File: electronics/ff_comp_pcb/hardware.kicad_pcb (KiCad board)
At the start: 4 copper layers, 60 x 37 mm, 92 parts, among them J1 Micro_SD_Card_Det_Hirose_DM3AT, J2 USB_A, J3 Conn_01x08_Female, U1 AS4C512M16D3L-12BIN, U2 A33, U3 FSUSB42MUX, U4 RTL8188CUS, U5 RTL8188CUS, Y1 24Mhz, Y2 32.768khz

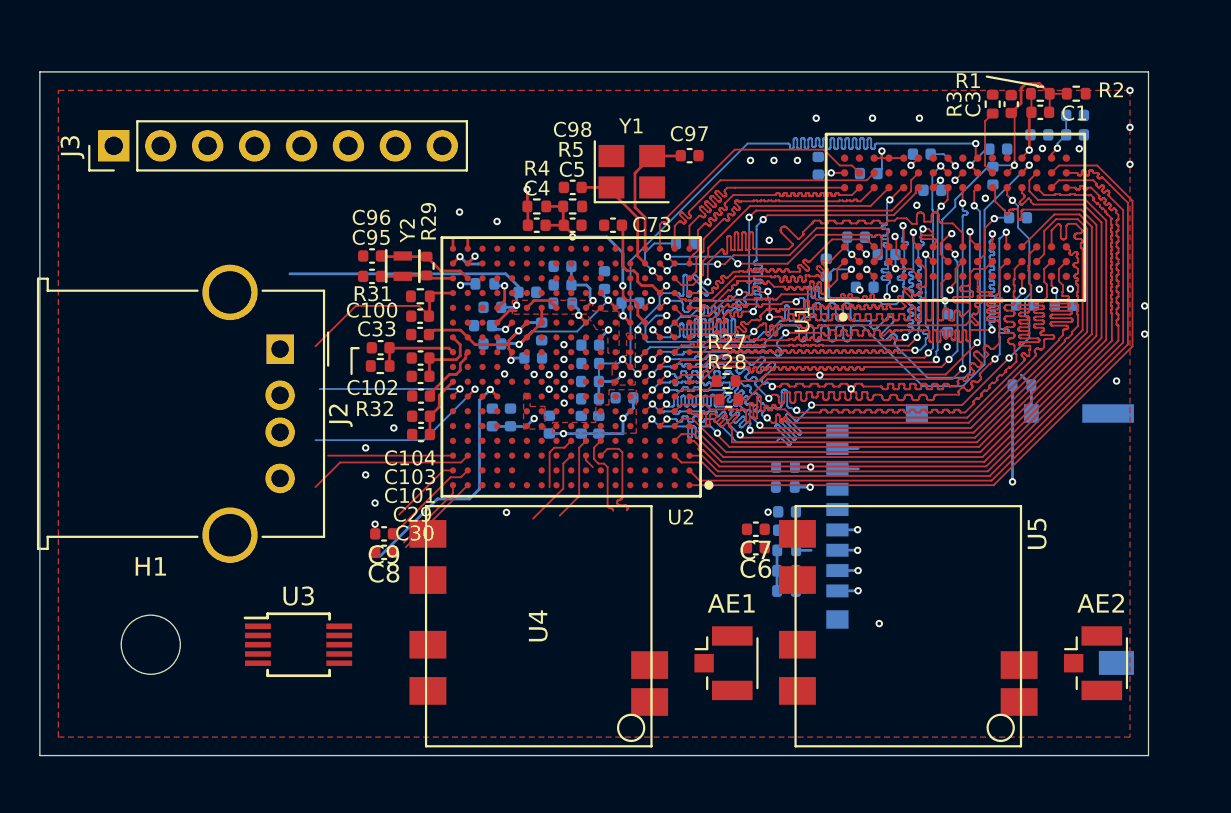
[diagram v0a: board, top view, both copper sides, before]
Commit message: Fit the board into the volume
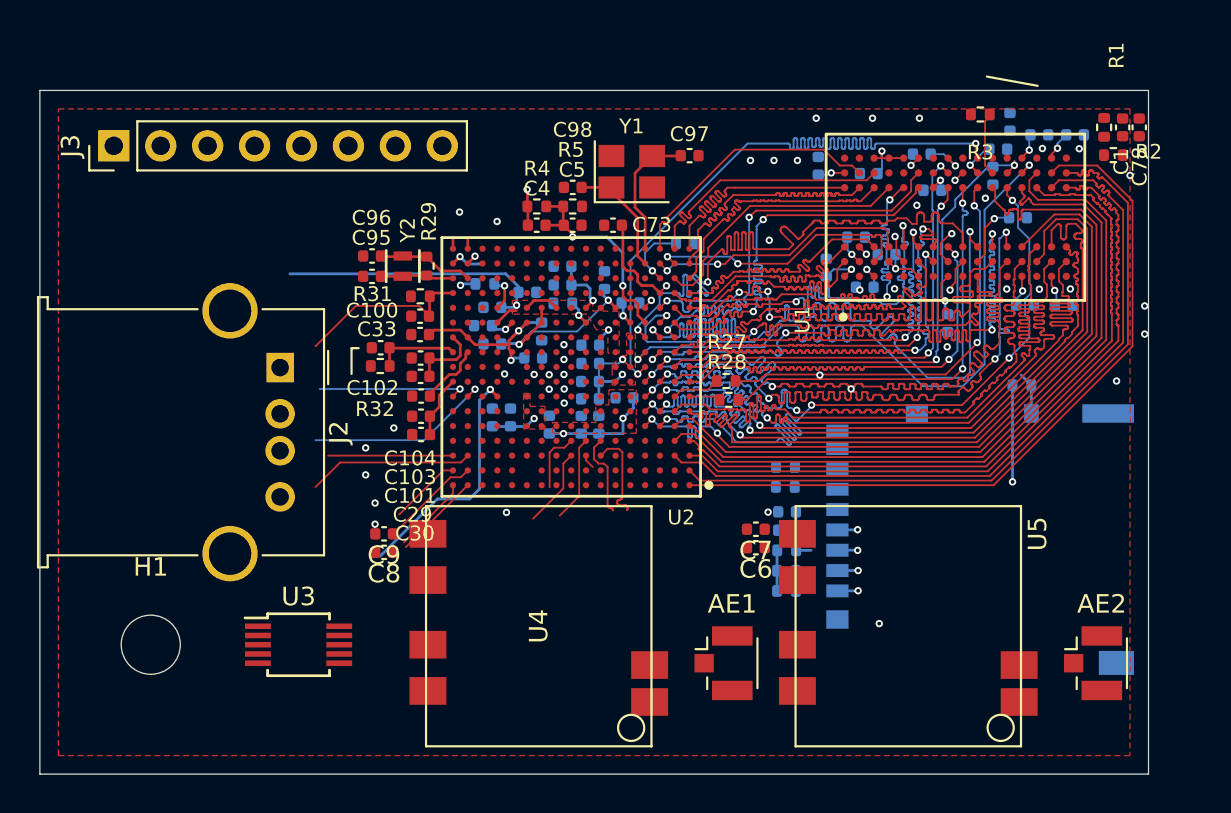
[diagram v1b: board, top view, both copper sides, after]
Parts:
- C3: moved to B.Cu
- C78: moved to F.Cu
- moved C1 4.53 mm to (144.6, 96.0), turned to 270 degrees
- moved R1 3.91 mm to (143.6, 96.0), turned to 270 degrees
- moved R2 3.88 mm to (144.1, 97.5)
- moved C78 3.54 mm to (145.5, 96.0), turned to 270 degrees
- moved J2 1.00 mm to (99.0, 109.0)
- moved C3 0.96 mm to (138.5, 95.7)
- moved R3 0.87 mm to (136.9, 95.3), turned to 0 degrees
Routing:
- net Net-(C1-Pad2): track 21.0 -> 13.0 mm
- net +1V35: track 43.1 -> 38.9 mm
- net /gpio/SD_DAT0: track 6.26 -> 4.29 mm, vias 1 -> 0
- net /gpio/SD_DAT1: track 5.29 -> 3.32 mm, vias 1 -> 0
- net GND: vias 46 -> 44

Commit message: Finished up the routing on the power board, still needs a double check.
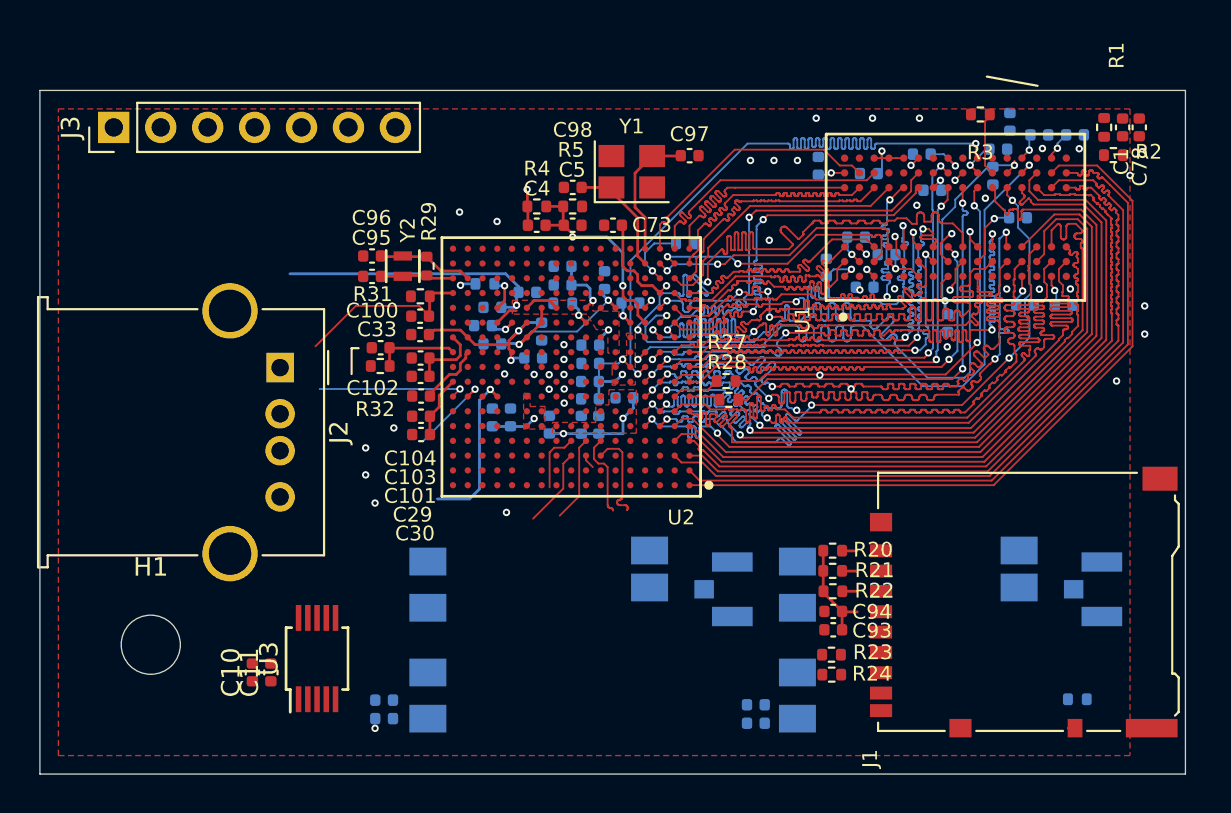
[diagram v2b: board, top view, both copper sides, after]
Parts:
- added C10: 100nF, Capacitor_SMD:C_0402_1005Metric, F.Cu at (97.5, 125.5)
- added C11: 100nF, Capacitor_SMD:C_0402_1005Metric, F.Cu at (98.5, 125.5)
- AE1, AE2, C6, C7, C8, C9, U4, U5: moved to B.Cu
- C93, C94, J1, R20, R21, R22, R23, R24: moved to F.Cu
- J3: value Conn_01x08_Female -> Conn_01x07_Female; footprint Connector_PinHeader_2.54mm:PinHeader_1x08_P2.54mm_Vertical -> Connector_PinHeader_2.54mm:PinHeader_1x07_P2.54mm_Vertical
- moved R25 17.3 mm to (142.1, 127.0)
- moved R24 11.5 mm to (128.9, 125.6)
- moved C7 10.5 mm to (124.8, 128.2)
- moved C9 10.0 mm to (104.6, 128.0)
- moved R23 9.42 mm to (128.8, 124.5)
- moved C6 8.50 mm to (124.8, 127.2)
- moved C8 8.00 mm to (104.6, 127.0)
- moved C93 6.86 mm to (128.9, 123.2)
- moved C94 5.05 mm to (128.9, 122.2)
- moved J1 4.12 mm to (139.2, 121.7), turned to 90 degrees
- moved AE1 4.00 mm to (123.0, 121.0)
- moved AE2 4.00 mm to (143.0, 121.0)
- moved R22 3.34 mm to (128.9, 121.1)
- moved R20 3.32 mm to (128.9, 118.9)
- moved R21 2.50 mm to (128.9, 120.0)
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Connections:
- J2 pad 1: +5V -> Net-(J2-Pad1)
- J2 pad 2: (no net) -> /gpio/MUX1-USB1-DN
- J2 pad 3: (no net) -> /gpio/MUX1-USB1-DP
- J2 pad 4: (no net) -> GND
- J2 pad 5: Net-(J2-Pad5) -> GND
- U1 pad J1: (no net) -> Net-(U1-PadJ1)
- U1 pad J9: (no net) -> Net-(U1-PadJ9)
- U1 pad L1: (no net) -> Net-(U1-PadL1)
- U1 pad L9: (no net) -> Net-(U1-PadL9)
- U2 pad A10: (no net) -> Net-(U2-PadA10)
- U2 pad A11: (no net) -> Net-(U2-PadA11)
- U2 pad A12: (no net) -> Net-(U2-PadA12)
- U2 pad A13: (no net) -> Net-(U2-PadA13)
- U2 pad A14: (no net) -> Net-(U2-PadA14)
- U2 pad A15: (no net) -> Net-(U2-PadA15)
- U2 pad A16: (no net) -> /gpio/PG8
- U2 pad A17: (no net) -> /gpio/PG6
- U2 pad A2: (no net) -> Net-(U2-PadA2)
- U2 pad A3: (no net) -> /gpio/MUX_~OE
- U2 pad A4: (no net) -> Net-(U2-PadA4)
- U2 pad A5: (no net) -> Net-(U2-PadA5)
- U2 pad A6: (no net) -> Net-(U2-PadA6)
- U2 pad A7: (no net) -> Net-(U2-PadA7)
- U2 pad A8: (no net) -> Net-(U2-PadA8)
- U2 pad A9: (no net) -> Net-(U2-PadA9)
- U2 pad B10: (no net) -> Net-(U2-PadB10)
- U2 pad B11: (no net) -> Net-(U2-PadB11)
- U2 pad B13: (no net) -> Net-(U2-PadB13)
- U2 pad B14: (no net) -> Net-(U2-PadB14)
- U2 pad B15: (no net) -> Net-(U2-PadB15)
- U2 pad B16: (no net) -> /gpio/PG9
- U2 pad B17: (no net) -> /gpio/PG7
- U2 pad B2: (no net) -> Net-(U2-PadB2)
- U2 pad B3: (no net) -> /gpio/MUX_SEL
- U2 pad B4: (no net) -> Net-(U2-PadB4)
- U2 pad B5: (no net) -> Net-(U2-PadB5)
- U2 pad B6: (no net) -> Net-(U2-PadB6)
- U2 pad B7: (no net) -> Net-(U2-PadB7)
- U2 pad B8: (no net) -> Net-(U2-PadB8)
- U2 pad B9: (no net) -> Net-(U2-PadB9)
- U2 pad C10: (no net) -> Net-(U2-PadC10)
- U2 pad C11: (no net) -> Net-(U2-PadC11)
- U2 pad C12: (no net) -> Net-(U2-PadC12)
- U2 pad C13: (no net) -> Net-(U2-PadC13)
- U2 pad C14: (no net) -> Net-(U2-PadC14)
- U2 pad C15: (no net) -> Net-(U2-PadC15)
- U2 pad C16: (no net) -> /gpio/PG11
- U2 pad C17: (no net) -> /gpio/PG10
- U2 pad C3: (no net) -> Net-(U2-PadC3)
- U2 pad C4: (no net) -> Net-(U2-PadC4)
- U2 pad C5: (no net) -> Net-(U2-PadC5)
- U2 pad C6: (no net) -> Net-(U2-PadC6)
- U2 pad D10: (no net) -> Net-(U2-PadD10)
- U2 pad D11: (no net) -> Net-(U2-PadD11)
- U2 pad D12: (no net) -> Net-(U2-PadD12)
- U2 pad D13: (no net) -> Net-(U2-PadD13)
- U2 pad D14: (no net) -> Net-(U2-PadD14)
- U2 pad D15: (no net) -> Net-(U2-PadD15)
- U2 pad D16: (no net) -> Net-(U2-PadD16)
- U2 pad D17: (no net) -> Net-(U2-PadD17)
- U2 pad D3: (no net) -> Net-(U2-PadD3)
- U2 pad D4: (no net) -> Net-(U2-PadD4)
- U2 pad D5: (no net) -> Net-(U2-PadD5)
- U2 pad D6: (no net) -> Net-(U2-PadD6)
- U2 pad E14: (no net) -> Net-(U2-PadE14)
- U2 pad E15: (no net) -> Net-(U2-PadE15)
- U2 pad E16: (no net) -> Net-(U2-PadE16)
- U2 pad E17: (no net) -> Net-(U2-PadE17)
- U2 pad F14: (no net) -> Net-(U2-PadF14)
- U2 pad F15: (no net) -> Net-(U2-PadF15)
- U2 pad F16: (no net) -> Net-(U2-PadF16)
- U2 pad F17: (no net) -> Net-(U2-PadF17)
- U2 pad G15: (no net) -> Net-(U2-PadG15)
- U2 pad G16: (no net) -> /gpio/UART0_RX
- U2 pad G17: (no net) -> /gpio/UART0_TX
- U2 pad H14: (no net) -> Net-(U2-PadH14)
- U2 pad H15: (no net) -> Net-(U2-PadH15)
- U2 pad H16: (no net) -> Net-(U2-PadH16)
- U2 pad J14: (no net) -> Net-(U2-PadJ14)
- U2 pad J15: (no net) -> Net-(U2-PadJ15)
- U2 pad J16: (no net) -> Net-(U2-PadJ16)
- U2 pad J17: (no net) -> Net-(U2-PadJ17)
- U2 pad K14: (no net) -> Net-(U2-PadK14)
- U2 pad K15: (no net) -> Net-(U2-PadK15)
- U2 pad L14: (no net) -> Net-(U2-PadL14)
- U2 pad L15: (no net) -> Net-(U2-PadL15)
- U2 pad L7: (no net) -> Net-(U2-PadL7)
- U2 pad M15: (no net) -> Net-(U2-PadM15)
- U2 pad M16: (no net) -> Net-(U2-PadM16)
- U2 pad M17: (no net) -> Net-(U2-PadM17)
- U2 pad N15: (no net) -> Net-(U2-PadN15)
- U2 pad N16: (no net) -> Net-(U2-PadN16)
- U2 pad N17: (no net) -> Net-(U2-PadN17)
- U2 pad N5: (no net) -> Net-(U2-PadN5)
- U2 pad N7: (no net) -> Net-(U2-PadN7)
- U2 pad P10: (no net) -> Net-(U2-PadP10)
- U2 pad P11: (no net) -> Net-(U2-PadP11)
- U2 pad P12: (no net) -> Net-(U2-PadP12)
- U2 pad P13: (no net) -> Net-(U2-PadP13)
- U2 pad P14: (no net) -> Net-(U2-PadP14)
- U2 pad P15: (no net) -> Net-(U2-PadP15)
- U2 pad P16: (no net) -> Net-(U2-PadP16)
- U2 pad P4: (no net) -> Net-(U2-PadP4)
- U2 pad P5: (no net) -> Net-(U2-PadP5)
- U2 pad P6: (no net) -> Net-(U2-PadP6)
- U2 pad P7: (no net) -> Net-(U2-PadP7)
- U2 pad P8: (no net) -> Net-(U2-PadP8)
- U2 pad P9: (no net) -> Net-(U2-PadP9)
- U2 pad R10: (no net) -> Net-(U2-PadR10)
- U2 pad R11: (no net) -> Net-(U2-PadR11)
- U2 pad R12: (no net) -> Net-(U2-PadR12)
- U2 pad R13: (no net) -> Net-(U2-PadR13)
- U2 pad R14: (no net) -> Net-(U2-PadR14)
- U2 pad R15: (no net) -> Net-(U2-PadR15)
- U2 pad R4: (no net) -> Net-(U2-PadR4)
- U2 pad R5: (no net) -> Net-(U2-PadR5)
- U2 pad R6: (no net) -> Net-(U2-PadR6)
- U2 pad R7: (no net) -> Net-(U2-PadR7)
- U2 pad R8: (no net) -> Net-(U2-PadR8)
- U2 pad R9: (no net) -> Net-(U2-PadR9)
- U2 pad T10: (no net) -> Net-(U2-PadT10)
- U2 pad T11: (no net) -> Net-(U2-PadT11)
- U2 pad T12: (no net) -> Net-(U2-PadT12)
- U2 pad T13: (no net) -> Net-(U2-PadT13)
- U2 pad T14: (no net) -> Net-(U2-PadT14)
- U2 pad T15: (no net) -> Net-(U2-PadT15)
- U2 pad T16: (no net) -> /gpio/USB0-DN
- U2 pad T17: (no net) -> /gpio/USB0-DP
- U2 pad T5: (no net) -> Net-(U2-PadT5)
- U2 pad T6: (no net) -> Net-(U2-PadT6)
- U2 pad T7: (no net) -> Net-(U2-PadT7)
- U2 pad T8: (no net) -> Net-(U2-PadT8)
- U2 pad T9: (no net) -> Net-(U2-PadT9)
- U2 pad U10: (no net) -> Net-(U2-PadU10)
- U2 pad U11: (no net) -> Net-(U2-PadU11)
- U2 pad U12: (no net) -> Net-(U2-PadU12)
- U2 pad U13: (no net) -> Net-(U2-PadU13)
- U2 pad U14: (no net) -> Net-(U2-PadU14)
- U2 pad U15: (no net) -> Net-(U2-PadU15)
- U2 pad U16: (no net) -> /gpio/USB1-DN
- U2 pad U17: (no net) -> /gpio/USB1-DP
- U2 pad U5: (no net) -> Net-(U2-PadU5)
- U2 pad U6: (no net) -> Net-(U2-PadU6)
- U2 pad U7: (no net) -> Net-(U2-PadU7)
- U2 pad U8: (no net) -> Net-(U2-PadU8)
- U2 pad U9: (no net) -> Net-(U2-PadU9)
- U3 pad 1: (no net) -> +3V3
- U3 pad 10: (no net) -> /gpio/MUX_~OE
- U3 pad 2: (no net) -> /gpio/MUX_SEL
- U3 pad 3: (no net) -> /gpio/USB1-DP
- U3 pad 4: (no net) -> /gpio/USB1-DN
- U3 pad 5: (no net) -> GND
- U3 pad 6: (no net) -> /gpio/MUX2-USB1-DN
- U3 pad 7: (no net) -> /gpio/MUX2-USB1-DP
- U3 pad 8: (no net) -> /gpio/MUX1-USB1-DN
- U3 pad 9: (no net) -> /gpio/MUX1-USB1-DP
- U4 pad 4: (no net) -> /gpio/MUX2-USB1-DN
- U4 pad 5: (no net) -> /gpio/MUX2-USB1-DP
- U5 pad 4: (no net) -> /gpio/USB0-DN
- U5 pad 5: (no net) -> /gpio/USB0-DP
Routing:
- net (no net): track 56.0 -> 0.00 mm, vias 4 -> 0
- net /gpio/UART0_TX: track 0.00 -> 8.16 mm, vias 0 -> 1
- net /gpio/SD_DET: track 15.4 -> 8.75 mm
- net +3V3: track 27.6 -> 21.3 mm, vias 6 -> 4
- net /gpio/UART0_RX: track 0.00 -> 4.45 mm, vias 0 -> 1
- net /gpio/SD_DAT3: track 6.51 -> 5.39 mm, vias 1 -> 0
- net /gpio/SD_DAT2: track 7.08 -> 5.97 mm, vias 1 -> 0
- net /gpio/SD_CMD: track 2.67 -> 1.59 mm, vias 1 -> 0
- net GND: vias 44 -> 42
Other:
- board size 60 x 37 mm -> 62 x 37 mm

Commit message: Power distrobution IP on the CPU board. Transistors in for 5V control. Part numbers in.
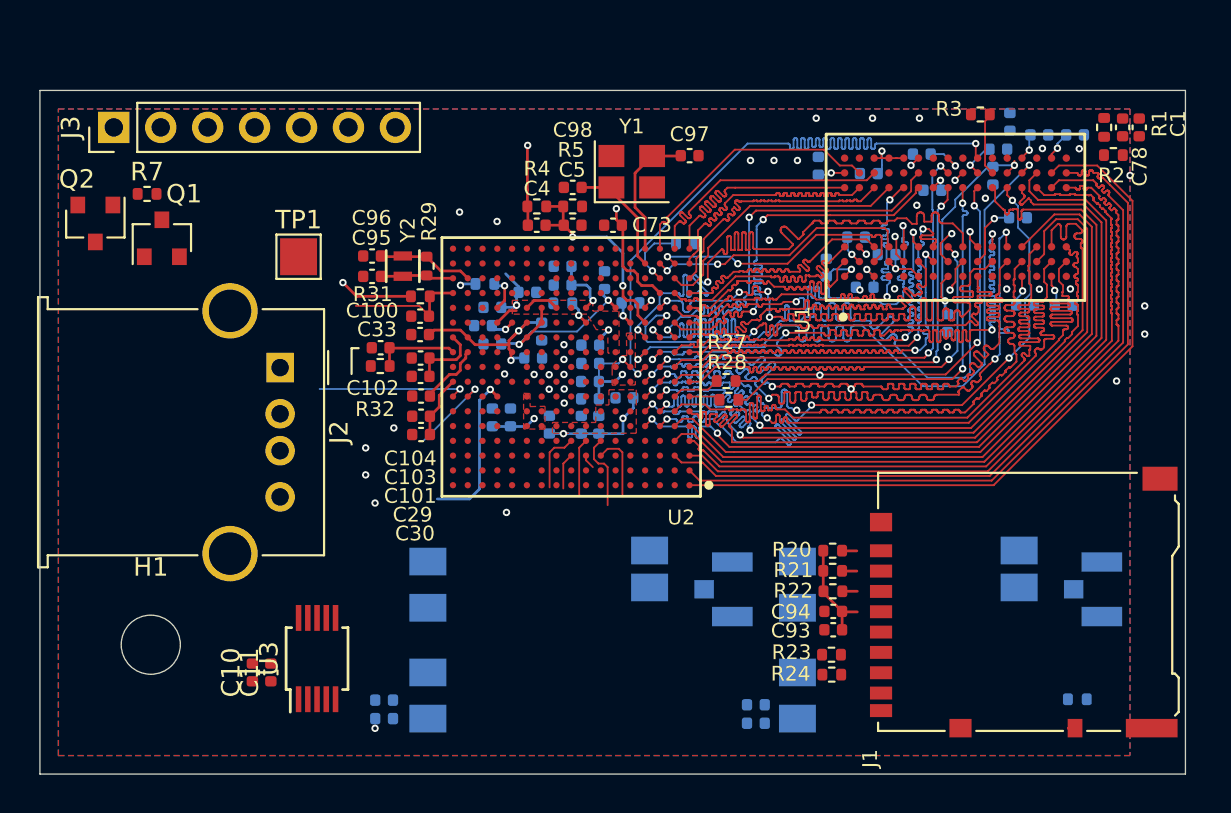
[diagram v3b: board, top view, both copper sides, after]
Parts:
- added Q1: Q_PMOS_GDS, Package_TO_SOT_SMD:SOT-23, F.Cu at (92.6, 102.0)
- added Q2: Q_NPN_BEC, Package_TO_SOT_SMD:SOT-23, F.Cu at (89.0, 101.2)
- added R7: 100k, Resistor_SMD:R_0402_1005Metric, F.Cu at (91.8, 99.6)
- added TP1: TestPoint, TestPoint:TestPoint_Pad_2.0x2.0mm, F.Cu at (100.0, 103.0)
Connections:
- net /gpio/PG10 renamed Net-(U2-PadC17)
- net /gpio/PG11 renamed Net-(U2-PadC16)
- net /gpio/PG8 renamed Net-(U2-PadA16)
- net /gpio/PG9 renamed Net-(U2-PadB16)
- J3 pad 5: +2V5 -> +1V1
- J3 pad 6: +1V35 -> +2V5
- J3 pad 7: +1V1 -> +1V35
- U2 pad A17: /gpio/PG6 -> /gpio/MUX_~OE
- U2 pad A3: /gpio/MUX_~OE -> Net-(U2-PadA3)
- U2 pad B17: /gpio/PG7 -> /gpio/MUX_SEL
- U2 pad B3: /gpio/MUX_SEL -> Net-(U2-PadB3)
- U2 pad U13: Net-(U2-PadU13) -> /gpio/VBUS_~EN
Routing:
- net +2V5: track 28.3 -> 45.1 mm
- net +1V1: track 28.4 -> 16.7 mm
- net +3V3: track 21.3 -> 27.5 mm, vias 4 -> 5
- net /gpio/RESET: track 9.72 -> 6.63 mm
- net +1V35: track 38.9 -> 41.3 mm
- net /gpio/SD_DAT0: track 4.29 -> 1.97 mm
- net /gpio/SD_CLK: track 4.64 -> 3.15 mm
- net /gpio/SD_DAT2: track 5.97 -> 4.62 mm
- added copper zone on In1.Cu, net +1V1
- added copper zone on In1.Cu, net +1V35
- added copper zone on In1.Cu, net +3V0
- added copper zone on In1.Cu, net +3V3
- added copper zone on B.Cu, net GND

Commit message: Routing the MCU board.
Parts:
- R25: moved to F.Cu
- moved R25 15.8 mm to (126.4, 128.6), turned to 270 degrees
- moved C10 1.40 mm to (97.5, 126.9)
- moved C11 1.40 mm to (98.5, 126.9)
- moved R20 1.31 mm to (128.9, 117.6)
- moved R21 1.00 mm to (128.9, 119.0)
- moved R24 0.78 mm to (128.9, 126.4)
- moved R22 0.71 mm to (128.9, 120.4)
- moved R23 0.66 mm to (128.8, 125.2)
- moved C94 0.60 mm to (128.9, 121.6)
- moved C93 0.60 mm to (128.9, 122.6)
- moved C6 0.45 mm to (124.3, 127.5)
- moved C7 0.45 mm to (124.3, 128.4)
- moved R7 0.20 mm to (92.0, 99.6)
- moved C8 0.20 mm to (104.4, 127.0)
- moved C9 0.20 mm to (104.4, 128.0)
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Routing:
- net +3V3: track 27.5 -> 97.4 mm, vias 5 -> 12
- net /gpio/USB0-DN: track 0.00 -> 40.1 mm, vias 0 -> 1
- net /gpio/USB0-DP: track 0.00 -> 37.4 mm, vias 0 -> 1
- net /gpio/SD_DET: track 8.75 -> 44.1 mm, vias 1 -> 0
- net /gpio/USB1-DN: track 0.00 -> 32.9 mm, vias 0 -> 2
- net /gpio/USB1-DP: track 0.00 -> 32.8 mm, vias 0 -> 2
- net /gpio/SD_DAT0: track 1.97 -> 28.3 mm
- net /gpio/VBUS_~EN: track 0.00 -> 25.2 mm
- net /gpio/SD_CMD: track 1.59 -> 26.4 mm
- net /gpio/SD_DAT1: track 3.32 -> 26.3 mm
- net +2V5: track 45.1 -> 22.4 mm
- net /gpio/SD_DAT2: track 4.62 -> 26.7 mm
- net /gpio/SD_DAT3: track 4.92 -> 26.5 mm
- net /gpio/SD_CLK: track 3.15 -> 24.0 mm
- net /gpio/MUX_SEL: track 0.00 -> 16.0 mm
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
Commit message: Finished layout.
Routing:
- net /gpio/RF1: track 0.00 -> 2.99 mm
- net /gpio/RF2: track 0.00 -> 2.99 mm
- net GND: vias 49 -> 47
